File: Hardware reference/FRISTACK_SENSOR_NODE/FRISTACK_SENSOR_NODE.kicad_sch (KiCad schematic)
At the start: 64 parts, among them J1 SPI_Header, J2 I2C/GPIO/I2S, J3 BATT, SW1 SW_Push, SW2 SW_Push, U1 ESP32-H2-MINI-1, Y1 32.768 kHz

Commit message: Power management changes on CORE and SENSOR_NODE
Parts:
- added C27: 4.7uF, Capacitor_SMD:C_0603_1608Metric, symbol Device:C
- added C28: 10uF, Capacitor_SMD:C_0603_1608Metric, symbol Device:C
- added L1: 2.2uH, Inductor_SMD:L_0805_2012Metric, symbol Device:L
- added R27: 267k, Resistor_SMD:R_0603_1608Metric, symbol Device:R
- added U2: TPS62840DLCR, User_imports:SON50P200X150X100-8N, symbol TPS62840DLCR:TPS62840DLCR
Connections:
- net +3V3: now also D2.1 (K)
- net GND: now also C27.2, C28.2, R27.2, U2.1 (GND), U2.3 (MODE), U2.6 (STOP)
- net at D2.2 (A): now also C28.1, L1.2, U2.8 (VOS); no longer J3.2 (Pin_2)
- net at U1.15 (VBAT): no longer D2.1 (K)
- new net: R27.1, U2.5 (VSET)
- new net: L1.1, U2.7 (SW)
- new net VBAT: C27.1, J3.2 (Pin_2), U2.2 (VIN), U2.4 (EN)
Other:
- moved on the sheet: C1, C10, C11, C12, C13, C14, C15, C16, C17, C18, C19, C2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

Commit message: Added logos, annotations
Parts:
- removed R13: 22, Resistor_SMD:R_0603_1608Metric, symbol Device:R
- C27, C28: footprint Capacitor_SMD:C_0603_1608Metric -> Capacitor_SMD:C_0402_1005Metric
- L1: footprint Inductor_SMD:L_0805_2012Metric -> User_imports:INDC2016X120N
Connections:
- net ADC1: now also J2.5 (Pin_5)
- net SDA1: now also R23.1
- removed net GPIO03: J2.5 (Pin_5), R23.1
- no-connect marks 1 -> 2
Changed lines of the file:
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@@
 	)
 	(no_connect
+		(at 248.92 161.29)
+	)
+	(no_connect
 		(at 179.07 134.62)
 	)
@@
 	(wire
 		(pts
-			(xy 261.62 161.29) (xy 264.16 161.29)
-		)
-		(stroke
-			(width 0)
-			(type default)
-		)
-	)
-	(wire
-		(pts
 			(xy 210.82 34.29) (xy 217.17 34.29)
 		)
@@
 	(wire
 		(pts
-			(xy 248.92 161.29) (xy 254 161.29)
-		)
-		(stroke
-			(width 0)
-			(type default)
-		)
-	)
-	(wire
-		(pts
 			(xy 290.83 156.21) (xy 248.92 156.21)
 		)
@@
 		)
 	)
-	(global_label "GPIO03"
-		(shape input)
-		(at 264.16 143.51 0)
-		(fields_autoplaced yes)
-		(effects
-			(font
-				(size 1.27 1.27)
-			)
-			(justify left)
-		)
-		(property "Intersheetrefs" "${INTERSHEET_REFS}"
-			(at 274.0395 143.51 0)
-			(effects
-				(font
-					(size 1.27 1.27)
-				)
-				(justify left)
-				(hide yes)
-			)
-		)
-	)
 	(global_label "ESP_PWR"
 		(shape input)
@@
 		)
 	)
-	(global_label "GPIO03"
+	(global_label "ADC1"
 		(shape input)
 		(at 367.03 135.89 0)
@@
 		)
 		(property "Intersheetrefs" "${INTERSHEET_REFS}"
-			(at 376.9095 135.89 0)
+			(at 374.8533 135.89 0)
 			(effects
 				(font
@@
 	(global_label "SDA1"
 		(shape input)
-		(at 264.16 161.29 0)
+		(at 264.16 143.51 0)
 		(fields_autoplaced yes)
 		(effects
@@
 		)
 		(property "Intersheetrefs" "${INTERSHEET_REFS}"
-			(at 271.9228 161.29 0)
+			(at 271.9228 143.51 0)
 			(effects
 				(font
@@
 			)
 		)
-		(property "Footprint" "Capacitor_SMD:C_0603_1608Metric"
+		(property "Footprint" "Capacitor_SMD:C_0402_1005Metric"
 			(at 313.3852 44.45 0)
 			(effects
@@
 	)
 	(symbol
-		(lib_id "Device:R")
-		(at 257.81 161.29 270)
-		(unit 1)
-		(exclude_from_sim no)
-		(in_bom yes)
-		(on_board yes)
-		(dnp no)
-		(property "Reference" "R13"
-			(at 262.382 162.814 90)
-			(effects
-				(font
-					(size 1.27 1.27)
-				)
-			)
-		)
-		(property "Value" "22"
-			(at 257.81 161.29 90)
-			(effects
-				(font
-					(size 1.27 1.27)
-				)
-			)
-		)
-		(property "Footprint" "Resistor_SMD:R_0603_1608Metric"
-			(at 257.81 159.512 90)
-			(effects
-				(font
-					(size 1.27 1.27)
-				)
-				(hide yes)
-			)
-		)
-		(property "Datasheet" "~"
-			(at 257.81 161.29 0)
-			(effects
-				(font
-					(size 1.27 1.27)
-				)
-				(hide yes)
-			)
-		)
-		(property "Description" "Resistor"
-			(at 257.81 161.29 0)
-			(effects
-				(font
-					(size 1.27 1.27)
-				)
-				(hide yes)
-			)
-		)
-		(pin "2"
-		)
-		(pin "1"
-		)
-		(instances
-			(project "FRISTACK_SENSOR_NODE"
-				(path "/93ea00fb-97ce-495e-ab13-c4af9b79c25e"
-					(reference "R13")
-					(unit 1)
-				)
-			)
-		)
-	)
-	(symbol
 		(lib_id "power:GND")
 		(at 168.91 46.99 0)
@@
 			)
 		)
-		(property "Footprint" "Capacitor_SMD:C_0603_1608Metric"
+		(property "Footprint" "Capacitor_SMD:C_0402_1005Metric"
 			(at 384.5052 46.99 0)
 			(effects
@@
 			)
 		)
-		(property "Footprint" "Inductor_SMD:L_0805_2012Metric"
+		(property "Footprint" "User_imports:INDC2016X120N"
 			(at 372.11 34.29 0)
 			(effects

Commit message: Added USBSwitch to Core and added first version of Compatibility
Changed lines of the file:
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@@
 (kicad_sch
-	(version 20231120)
+	(version 20250114)
 	(generator "eeschema")
-	(generator_version "8.0")
+	(generator_version "9.0")
 	(paper "A3")
 	(junction
@@
 		)
 	)
+	(embedded_fonts no)
 )

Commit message: review and new BATTERY board
IOT - changed twai termination from header to switch option, new holes , added power planes
SENSOR NODE - new holes and back silk text
CORE - vertical twai termination header changed to horizontal
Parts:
- U2: footprint User_imports:SON50P200X150X100-8N -> TPS62840DLCR:SON50P200X150X100-8N
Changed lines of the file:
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@@
 			)
 		)
-		(property "Footprint" "User_imports:SON50P200X150X100-8N"
+		(property "Footprint" "TPS62840DLCR:SON50P200X150X100-8N"
 			(at 346.71 46.99 0)
 			(effects

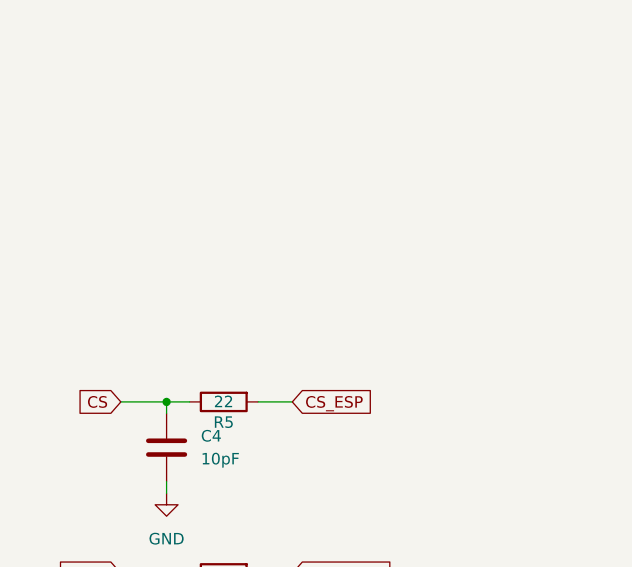
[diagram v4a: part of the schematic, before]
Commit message: Changes to Core and Sensor Node
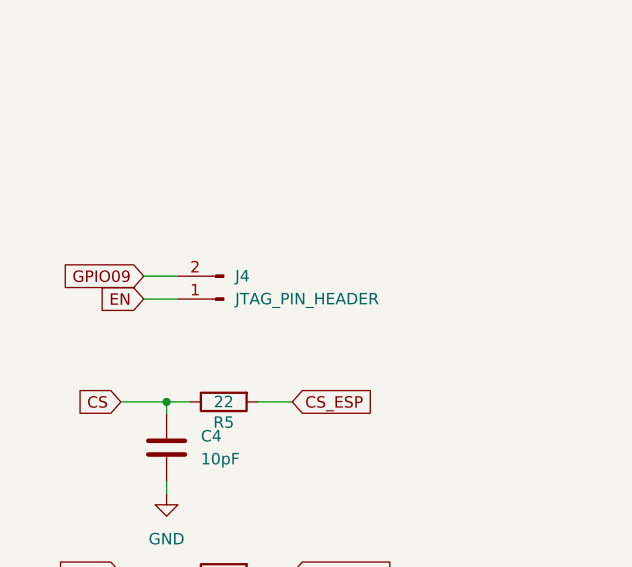
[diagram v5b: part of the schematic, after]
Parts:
- added J4: JTAG_PIN_HEADER, Connector_PinHeader_2.54mm:PinHeader_1x02_P2.54mm_Horizontal, symbol Connector:Conn_01x02_Pin
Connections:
- net EN: now also J4.1 (Pin_1)
- net GPIO09: now also J4.2 (Pin_2)
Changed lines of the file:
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@@
 	(wire
 		(pts
+			(xy 34.29 87.63) (xy 38.1 87.63)
+		)
+		(stroke
+			(width 0)
+			(type default)
+		)
+	)
+	(wire
+		(pts
 			(xy 346.71 229.87) (xy 350.52 229.87)
 		)
@@
 	(wire
 		(pts
+			(xy 34.29 90.17) (xy 38.1 90.17)
+		)
+		(stroke
+			(width 0)
+			(type default)
+		)
+	)
+	(wire
+		(pts
 			(xy 364.49 34.29) (xy 368.3 34.29)
 		)
@@
 		)
 	)
+	(global_label "EN"
+		(shape input)
+		(at 34.29 90.17 180)
+		(fields_autoplaced yes)
+		(effects
+			(font
+				(size 1.27 1.27)
+			)
+			(justify right)
+		)
+		(property "Intersheetrefs" "${INTERSHEET_REFS}"
+			(at 28.8253 90.17 0)
+			(effects
+				(font
+					(size 1.27 1.27)
+				)
+				(justify right)
+				(hide yes)
+			)
+		)
+	)
 	(global_label "UART0_RX"
 		(shape input)
@@
 		)
 	)
+	(global_label "GPIO09"
+		(shape input)
+		(at 34.29 87.63 180)
+		(fields_autoplaced yes)
+		(effects
+			(font
+				(size 1.27 1.27)
+			)
+			(justify right)
+		)
+		(property "Intersheetrefs" "${INTERSHEET_REFS}"
+			(at 24.4105 87.63 0)
+			(effects
+				(font
+					(size 1.27 1.27)
+				)
+				(justify right)
+				(hide yes)
+			)
+		)
+	)
 	(global_label "VBAT"
 		(shape input)
@@
 					(unit 1)
 				)
+			)
+		)
+	)
+	(symbol
+		(lib_id "Connector:Conn_01x02_Pin")
+		(at 43.18 90.17 180)
+		(unit 1)
+		(exclude_from_sim no)
+		(in_bom yes)
+		(on_board yes)
+		(dnp no)
+		(fields_autoplaced yes)
+		(property "Reference" "J4"
+			(at 44.45 87.6299 0)
+			(effects
+				(font
+					(size 1.27 1.27)
+				)
+				(justify right)
+			)
+		)
+		(property "Value" "JTAG_PIN_HEADER"
+			(at 44.45 90.1699 0)
+			(effects
+				(font
+					(size 1.27 1.27)
+				)
+				(justify right)
+			)
+		)
+		(property "Footprint" "Connector_PinHeader_2.54mm:PinHeader_1x02_P2.54mm_Horizontal"
+			(at 43.18 90.17 0)
+			(effects
+				(font
+					(size 1.27 1.27)
+				)
+				(hide yes)
+			)
+		)
+		(property "Datasheet" "~"
+			(at 43.18 90.17 0)
+			(effects
+				(font
+					(size 1.27 1.27)
+				)
+				(hide yes)
+			)
+		)
+		(property "Description" "Generic connector, single row, 01x02, script generated"
+			(at 43.18 90.17 0)
+			(effects
+				(font
+					(size 1.27 1.27)
+				)
+				(hide yes)
+			)
+		)
+		(pin "1"
+		)
+		(pin "2"
+		)
+		(instances
+			(project "FRISTACK_SENSOR_NODE"
+				(path "/93ea00fb-97ce-495e-ab13-c4af9b79c25e"
+					(reference "J4")
+					(unit 1)
+				)
